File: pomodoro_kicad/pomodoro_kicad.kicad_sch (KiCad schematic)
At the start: 15 parts, among them J1 USB_C_Receptacle_USB2.0_14P, SW2 SW_Push, SW3 SW_Push, U1 ESP32-S3-WROOM-1-N16R8, U2 AP2112K-3.3

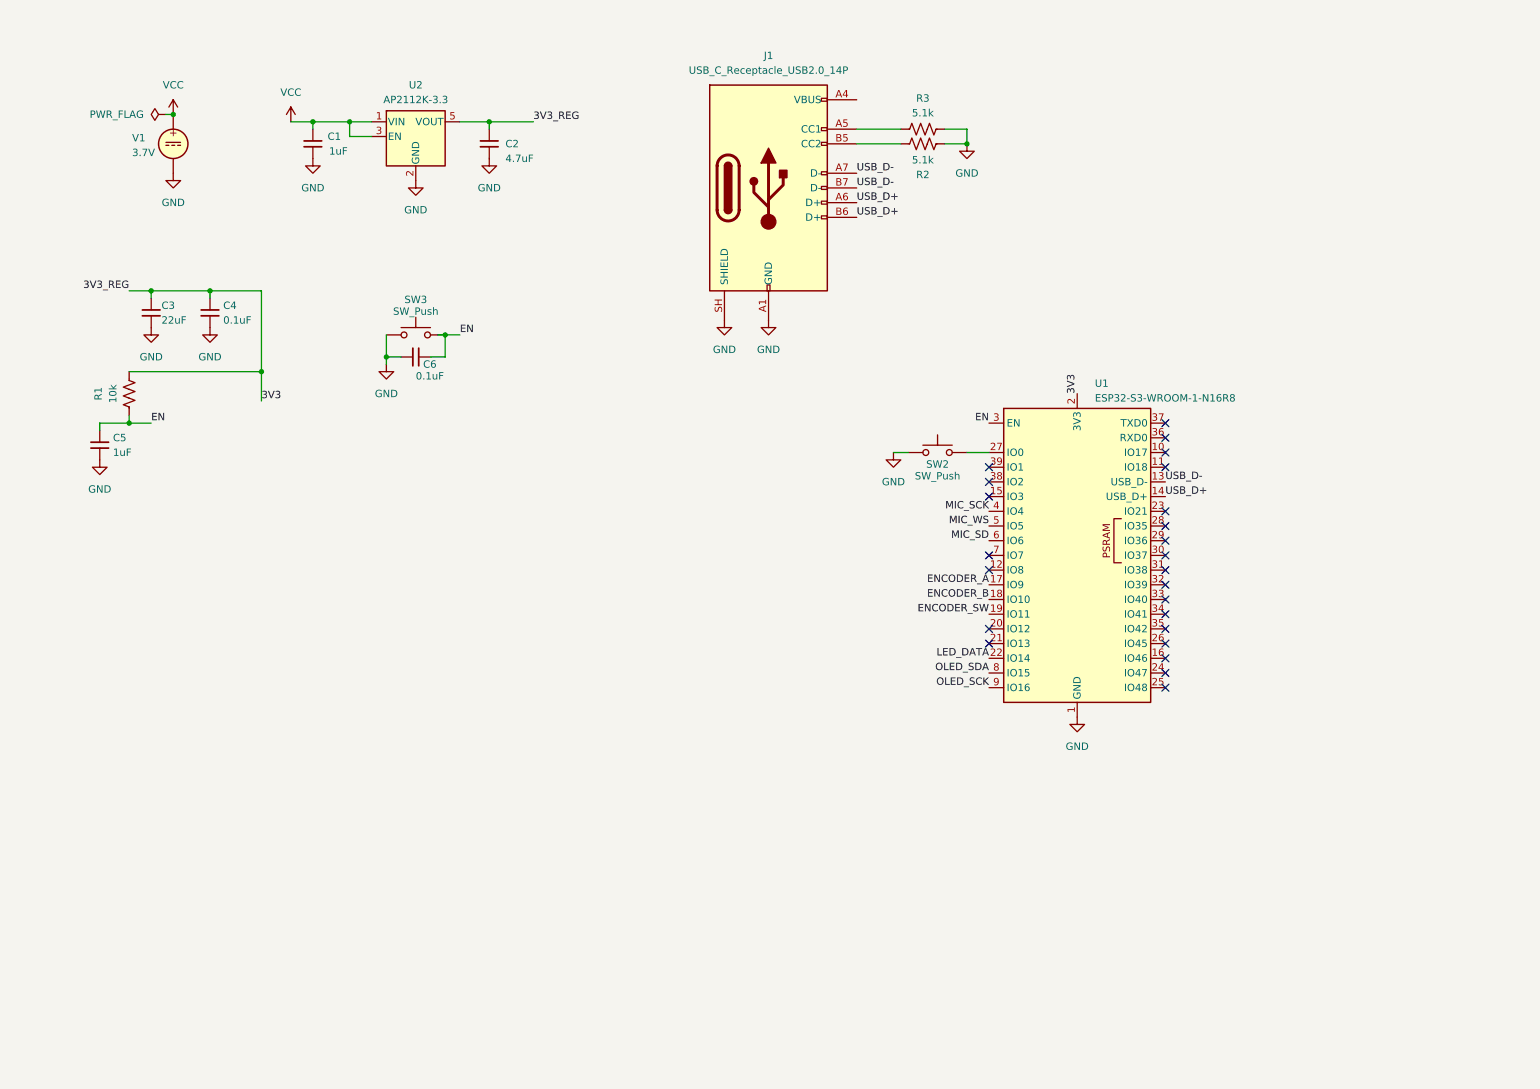
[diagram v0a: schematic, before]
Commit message: Schematic: Add OLED and rotary encoder
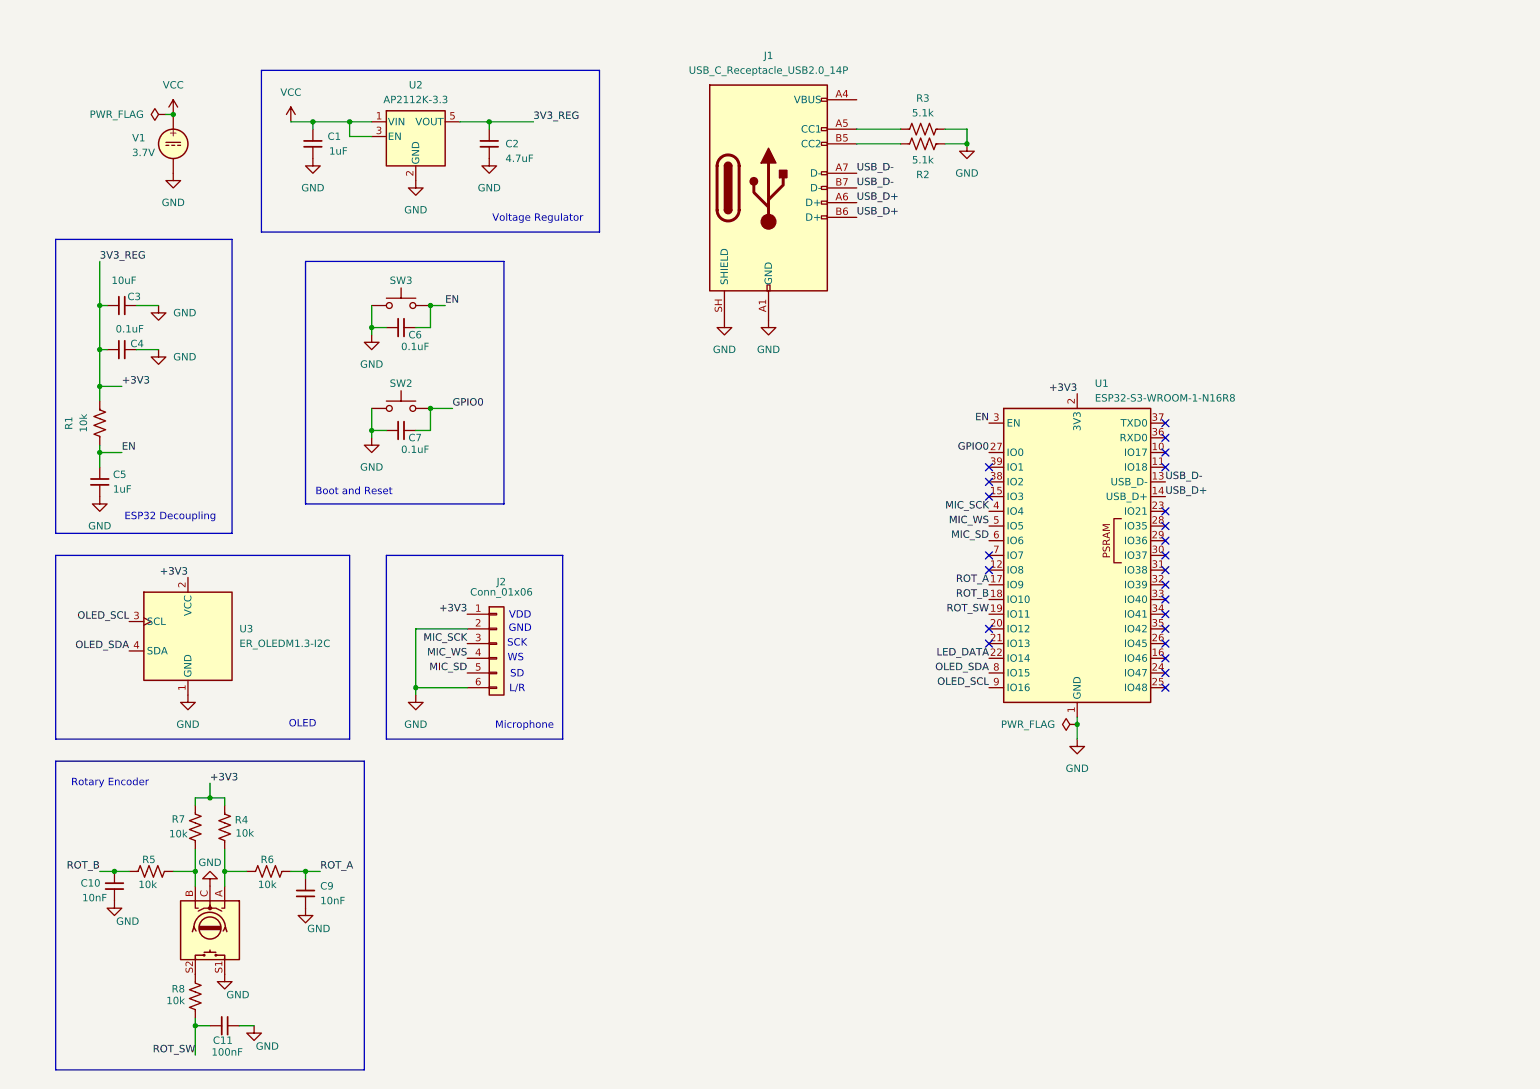
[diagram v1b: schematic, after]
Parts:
- added C10, C9: 10nF, symbol Device:C_Small
- added C11: 100nF, symbol Device:C_Small
- added C7: 0.1uF, symbol Device:C_Small
- added J2: Conn_01x06, Package_DIP:DIP-20_W7.62mm, symbol Connector_Generic:Conn_01x06
- added R4, R5, R6, R7, R8: 10k, Resistor_THT:R_Array_SIP4, symbol Device:R_US
- added SW1: RotaryEncoder_Switch, symbol Device:RotaryEncoder_Switch
- added U3: ER_OLEDM1.3-I2C, Display:ER_OLEDM0.91_1x-I2C, symbol Display_Graphic:ER_OLEDM0.91_1x-I2C
- C3: value 22uF -> 10uF
- SW2, SW3: value SW_Push -> (none)
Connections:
- net GND: now also C10.1, C11.1, C7.2, C9.1, J2.2 (Pin_2), J2.6 (Pin_6), SW1.C, SW1.S1, U3.1 (GND)
- net MIC_SCK: now also J2.3 (Pin_3)
- net MIC_SD: now also J2.5 (Pin_5)
- net MIC_WS: now also J2.4 (Pin_4)
- net OLED_SDA: now also U3.4 (SDA)
- net GPIO0: now reaches SW2.2, U1.27 (IO0)
- net GPIO0: now also C7.1
- net 3V3 renamed +3V3
- net +3V3: now also J2.1 (Pin_1), R4.1, R7.1, U3.2 (VCC)
- net ENCODER_A renamed ROT_A
- net ROT_A: now also C9.2, R6.1
- net ENCODER_B renamed ROT_B
- net ROT_B: now also C10.2, R5.1
- net ENCODER_SW renamed ROT_SW
- net ROT_SW: now also C11.2, R8.1
- net OLED_SCK renamed OLED_SCL
- net OLED_SCL: now also U3.3 (SCL)
- new net: R4.2, R6.2, SW1.A
- new net: R5.2, R7.2, SW1.B
- new net: R8.2, SW1.S2
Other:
- note added: "Boot and Reset"
- note added: "ESP32 Decoupling"
- note added: "GND"
- note added: "L/R"
- note added: "Microphone"
- note added: "OLED"
- note added: "Rotary Encoder"
- note added: "SCK"
- note added: "SD"
- note added: "VDD"
- note added: "Voltage Regulator"
- note added: "WS"
- moved on the sheet: C3, C4, C5, C6, R1, SW2, SW3

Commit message: Finish schematic, assign footprints, draft PCB layout
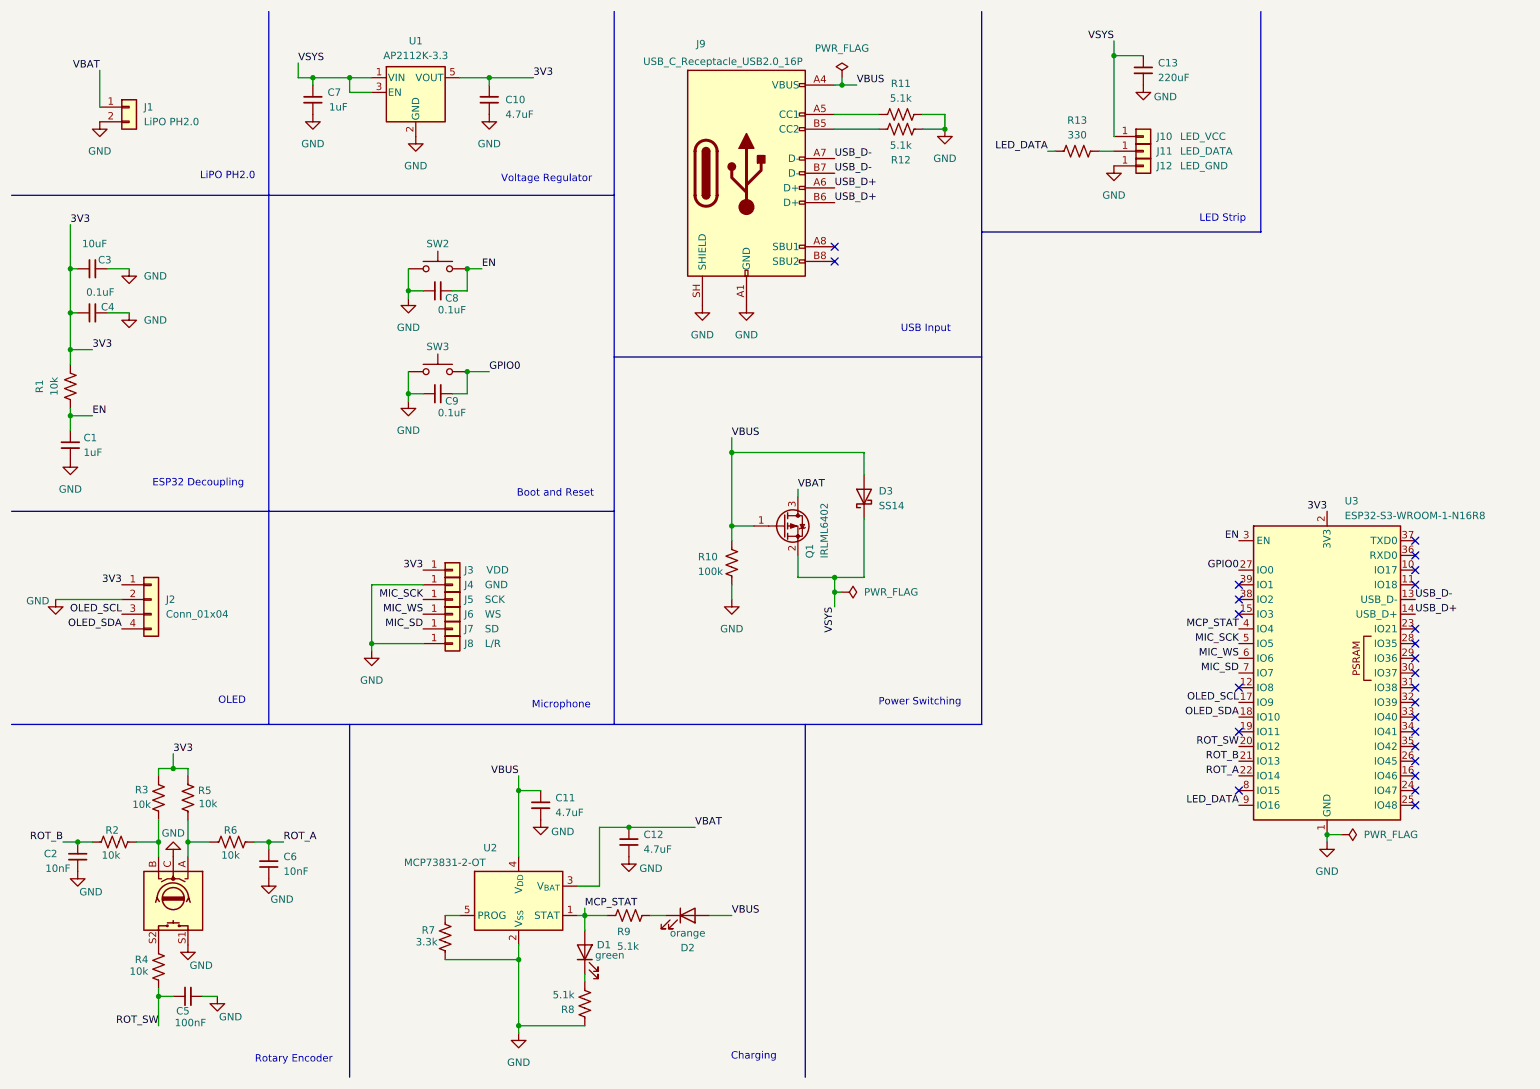
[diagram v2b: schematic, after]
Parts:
- removed J1: USB_C_Receptacle_USB2.0_14P, symbol Connector:USB_C_Receptacle_USB2.0_14P
- removed J2: Conn_01x06, Package_DIP:DIP-20_W7.62mm, symbol Connector_Generic:Conn_01x06
- removed U3: ER_OLEDM1.3-I2C, Display:ER_OLEDM0.91_1x-I2C, symbol Display_Graphic:ER_OLEDM0.91_1x-I2C
- removed V1: 3.7V, Package_SO:SOIC-8_3.9x4.9mm_P1.27mm, symbol Simulation_SPICE:VDC
- added C11, C12: 4.7uF, Capacitor_SMD:C_0603_1608Metric, symbol Device:C_Small
- added C13: 220uF, Capacitor_SMD:C_0603_1608Metric, symbol Device:C_Small
- added D1: green, LED_SMD:LED_0603_1608Metric, symbol Device:LED
- added D2: orange, LED_SMD:LED_0603_1608Metric, symbol Device:LED
- added D3: SS14, Diode_SMD:D_SMA, symbol Diode:SS14
- added J1: LiPO PH2.0, Connector_JST:JST_PH_B2B-PH-K_1x02_P2.00mm_Vertical, symbol Connector_Generic:Conn_01x02
- added J10: LED_VCC, TestPoint:TestPoint_THTPad_D2.0mm_Drill1.0mm, symbol Connector_Generic:Conn_01x01
- added J11: LED_DATA, TestPoint:TestPoint_THTPad_D2.0mm_Drill1.0mm, symbol Connector_Generic:Conn_01x01
- added J12: LED_GND, TestPoint:TestPoint_THTPad_D2.0mm_Drill1.0mm, symbol Connector_Generic:Conn_01x01
- added J2: Conn_01x04, Connector_PinSocket_2.54mm:PinSocket_1x04_P2.54mm_Vertical, symbol Connector_Generic:Conn_01x04
- added J3: VDD, TestPoint:TestPoint_THTPad_D2.0mm_Drill1.0mm, symbol Connector_Generic:Conn_01x01
- added J4: GND, TestPoint:TestPoint_THTPad_D2.0mm_Drill1.0mm, symbol Connector_Generic:Conn_01x01
- added J5: SCK, TestPoint:TestPoint_THTPad_D2.0mm_Drill1.0mm, symbol Connector_Generic:Conn_01x01
- added J6: WS, TestPoint:TestPoint_THTPad_D2.0mm_Drill1.0mm, symbol Connector_Generic:Conn_01x01
- added J7: SD, TestPoint:TestPoint_THTPad_D2.0mm_Drill1.0mm, symbol Connector_Generic:Conn_01x01
- added J8: L/R, TestPoint:TestPoint_THTPad_D2.0mm_Drill1.0mm, symbol Connector_Generic:Conn_01x01
- added J9: USB_C_Receptacle_USB2.0_16P, Connector_USB:USB_C_Receptacle_HRO_TYPE-C-31-M-12, symbol Connector:USB_C_Receptacle_USB2.0_16P
- added Q1: IRLML6402, Package_TO_SOT_SMD:SOT-23, symbol Transistor_FET:IRLML6402
- added R10: 100k, Resistor_SMD:R_0603_1608Metric, symbol Device:R_US
- added R13: 330, Resistor_SMD:R_0603_1608Metric, symbol Device:R_US
- added R7: 3.3k, Resistor_SMD:R_0603_1608Metric, symbol Device:R_US
- added R8, R9: 5.1k, Resistor_SMD:R_0603_1608Metric, symbol Device:R_US
- added U2: MCP73831-2-OT, Package_TO_SOT_SMD:SOT-23-5, symbol Battery_Management:MCP73831-2-OT
- C1: renamed from C5; footprint (none) -> Capacitor_SMD:C_0603_1608Metric
- C10: renamed from C2; footprint (none) -> Capacitor_SMD:C_0603_1608Metric
- C2: renamed from C10; footprint (none) -> Capacitor_SMD:C_0603_1608Metric
- C3, C4: footprint (none) -> Capacitor_SMD:C_0603_1608Metric
- C5: renamed from C11; footprint (none) -> Capacitor_SMD:C_0603_1608Metric
- C6: renamed from C9; footprint (none) -> Capacitor_SMD:C_0603_1608Metric
- C7: renamed from C1; footprint (none) -> Capacitor_SMD:C_0603_1608Metric
- C8: renamed from C6; footprint (none) -> Capacitor_SMD:C_0603_1608Metric
- C9: renamed from C7; footprint (none) -> Capacitor_SMD:C_0603_1608Metric
- R1: footprint (none) -> Resistor_SMD:R_0603_1608Metric
- R11: renamed from R3; footprint (none) -> Resistor_SMD:R_0603_1608Metric
- R12: renamed from R2; footprint (none) -> Resistor_SMD:R_0603_1608Metric
- R2: renamed from R5; footprint Resistor_THT:R_Array_SIP4 -> Resistor_SMD:R_0603_1608Metric
- R3: renamed from R7; footprint Resistor_THT:R_Array_SIP4 -> Resistor_SMD:R_0603_1608Metric
- R4: renamed from R8; footprint Resistor_THT:R_Array_SIP4 -> Resistor_SMD:R_0603_1608Metric
- R5: renamed from R4; footprint Resistor_THT:R_Array_SIP4 -> Resistor_SMD:R_0603_1608Metric
- R6: footprint Resistor_THT:R_Array_SIP4 -> Resistor_SMD:R_0603_1608Metric
- SW1: footprint (none) -> customFootprints:rotaryEncoder
- SW2: renamed from SW3; footprint Package_TO_SOT_THT:TO-220-3_Vertical -> Button_Switch_SMD:SW_SPST_PTS645Sx43SMTR92
- SW3: renamed from SW2; footprint Package_TO_SOT_THT:TO-220-3_Vertical -> Button_Switch_SMD:SW_SPST_PTS645Sx43SMTR92
- renumbered U2 to U1, U1 to U3
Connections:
- net GND: now also C11.2, C12.2, C13.2, J1.2 (Pin_2), J12.1 (Pin_1), J2.2 (Pin_2), J4.1 (Pin_1), J8.1 (Pin_1), J9.A1 (GND), J9.A12 (GND), J9.B1 (GND), J9.B12 (GND), J9.SH (SHIELD), R10.2, R7.1, R8.2, U2.2 (V_{SS})
- net LED_DATA: now also U3.9 (IO16), R13.2; no longer U3.22 (IO14)
- net MIC_SCK: now also U3.5 (IO5), J5.1 (Pin_1); no longer U3.4 (IO4)
- net MIC_SD: now also U3.7 (IO7), J7.1 (Pin_1); no longer U3.6 (IO6)
- net MIC_WS: now also U3.6 (IO6), J6.1 (Pin_1); no longer U3.5 (IO5)
- net OLED_SCL: now also U3.17 (IO9), J2.3 (Pin_3); no longer U3.9 (IO16)
- net OLED_SDA: now also U3.18 (IO10), J2.4 (Pin_4); no longer U3.8 (IO15)
- net ROT_A: now also U3.22 (IO14); no longer U3.17 (IO9)
- net ROT_B: now also U3.21 (IO13); no longer U3.18 (IO10)
- net ROT_SW: now also U3.20 (IO12); no longer U3.19 (IO11)
- net USB_D+: now also J9.A6 (D+), J9.B6 (D+)
- net USB_D-: now also J9.A7 (D-), J9.B7 (D-)
- net at R11.2: now also J9.A5 (CC1)
- net at R12.1: now also J9.B5 (CC2)
- net +3V3 renamed 3V3
- net 3V3: now also J2.1 (Pin_1), J3.1 (Pin_1)
- net VCC renamed VSYS
- net VSYS: now also C13.1, D3.1 (K), J10.1 (Pin_1), Q1.2 (S)
- new net: D2.1 (K), R9.2
- new net: J11.1 (Pin_1), R13.1
- new net: D1.1 (K), R8.1
- new net: R7.2, U2.5 (PROG)
- new net MCP_STAT: D1.2 (A), R9.1, U2.1 (STAT), U3.4 (IO4)
- new net VBAT: C12.1, J1.1 (Pin_1), Q1.3 (D), U2.3 (V_{BAT})
- new net VBUS: C11.1, D2.2 (A), D3.2 (A), J9.A4 (VBUS), J9.A9 (VBUS), J9.B4 (VBUS), J9.B9 (VBUS), Q1.1 (G), R10.1, U2.4 (V_{DD})
- no-connect marks 24 -> 25
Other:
- note added: "Charging"
- note added: "LED Strip"
- note added: "LiPO PH2.0"
- note added: "Power Switching"
- note added: "USB Input"
- note removed: "GND"
- note removed: "L/R"
- note removed: "SCK"
- note removed: "SD"
- note removed: "VDD"
- note removed: "WS"
- moved on the sheet: C1, C10, C2, C3, C4, C5, C6, C7, C8, C9, R1, R11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
